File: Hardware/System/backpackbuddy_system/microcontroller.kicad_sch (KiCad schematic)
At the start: 10 parts

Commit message: more changes
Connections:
- net PD2 renamed PD2/RX
- net PD3 renamed PD3/TX
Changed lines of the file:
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@@
     (effects (font (size 1.27 1.27)) (justify left))
   )
-  (hierarchical_label "PD2" (shape bidirectional) (at 177.8 88.9 0)
+  (hierarchical_label "PD2{slash}RX" (shape bidirectional) (at 177.8 88.9 0)
     (effects (font (size 1.27 1.27)) (justify left))
   )
@@
     (effects (font (size 1.27 1.27)) (justify right))
   )
-  (hierarchical_label "PD3" (shape bidirectional) (at 177.8 91.44 0)
+  (hierarchical_label "PD3{slash}TX" (shape bidirectional) (at 177.8 91.44 0)
     (effects (font (size 1.27 1.27)) (justify left))
   )

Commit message: labels and stuff almost done
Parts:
- C? (x2): value 100nF -> 0.1uF; footprint (none) -> Capacitor_SMD:C_0603_1608Metric_Pad1.08x0.95mm_HandSolder; MPN (none) -> CAP CER 0.1UF 50V X7R 0603; Stock (none) -> https://www.digikey.com/en/products/detail/kemet/C0603C104K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
- C?: footprint (none) -> Capacitor_SMD:C_0805_2012Metric_Pad1.18x1.45mm_HandSolder; MPN (none) -> CAP CER 0805 1UF 16V X7R 5%; Stock (none) -> https://www.digikey.com/en/products/detail/kemet/C0805C105J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
- C? (x2): footprint (none) -> Capacitor_SMD:C_0805_2012Metric_Pad1.18x1.45mm_HandSolder; MPN (none) -> CAP CER 10PF 100V X8R 0805; Stock (none) -> https://www.digikey.com/en/products/detail/kemet/C0805C100J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
- R?: footprint (none) -> Resistor_SMD:R_0603_1608Metric_Pad0.98x0.95mm_HandSolder; MPN (none) -> RES 10K OHM 1% 1/10W 0603; Stock (none) -> https://www.digikey.com/en/products/detail/vishay-dale/CRCW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
- SW?: footprint (none) -> BackpackBuddyFootprintLibrary:RST_SW; MPN (none) -> HP0315AFKP2-R; Stock (none) -> https://www.digikey.com/en/products/detail/nkk-switches/HP0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
- U?: Stock (none) -> Ordered!
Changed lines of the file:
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@@
     (in_bom yes) (on_board yes)
     (property "Reference" "C?" (id 0) (at 139.7 26.67 0))
-    (property "Value" "100nF" (id 1) (at 139.7 29.21 0))
-    (property "Footprint" "" (id 2) (at 135.5852 31.75 0)
+    (property "Value" "0.1uF" (id 1) (at 139.7 29.21 0))
+    (property "Footprint" "Capacitor_SMD:C_0603_1608Metric_Pad1.08x0.95mm_HandSolder" (id 2) (at 135.5852 31.75 0)
       (effects (font (size 1.27 1.27)) hide)
     )
     (property "Datasheet" "~" (id 3) (at 134.62 27.94 0)
+      (effects (font (size 1.27 1.27)) hide)
+    )
+    (property "MPN" "CAP CER 0.1UF 50V X7R 0603" (id 4) (at 134.62 27.94 0)
+      (effects (font (size 1.27 1.27)) hide)
+    )
+    (property "Stock" "https://www.digikey.com/en/products/detail/kemet/C0603C104K5RAC3190/12701955?utm_adgroup=Capacitors&utm_source=google&utm_medium=cpc&utm_campaign=Shopping_Supplier_KEMET&utm_term=&utm_content=Capacitors" (id 5) (at 134.62 27.94 0)
       (effects (font (size 1.27 1.27)) hide)
     )
@@
     (property "Reference" "C?" (id 0) (at 133.35 90.17 0))
     (property "Value" "1uF" (id 1) (at 133.35 92.71 0))
-    (property "Footprint" "" (id 2) (at 129.2352 95.25 0)
+    (property "Footprint" "Capacitor_SMD:C_0805_2012Metric_Pad1.18x1.45mm_HandSolder" (id 2) (at 129.2352 95.25 0)
       (effects (font (size 1.27 1.27)) hide)
     )
     (property "Datasheet" "~" (id 3) (at 128.27 91.44 0)
+      (effects (font (size 1.27 1.27)) hide)
+    )
+    (property "MPN" "CAP CER 0805 1UF 16V X7R 5%" (id 4) (at 128.27 91.44 0)
+      (effects (font (size 1.27 1.27)) hide)
+    )
+    (property "Stock" "https://www.digikey.com/en/products/detail/kemet/C0805C105J4RECAUTO/13228798?utm_adgroup=Capacitors&utm_source=google&utm_medium=cpc&utm_campaign=Shopping_Supplier_KEMET&utm_term=&utm_content=Capacitors" (id 5) (at 128.27 91.44 0)
       (effects (font (size 1.27 1.27)) hide)
     )
@@
     )
     (property "Datasheet" "http://ww1.microchip.com/downloads/en/DeviceDoc/Atmel-7766-8-bit-AVR-ATmega16U4-32U4_Datasheet.pdf" (id 3) (at 152.4 91.44 0)
+      (effects (font (size 1.27 1.27)) hide)
+    )
+    (property "Stock" "Ordered!" (id 4) (at 152.4 91.44 0)
       (effects (font (size 1.27 1.27)) hide)
     )
@@
       (effects (font (size 1.27 1.27)) (justify left))
     )
-    (property "Footprint" "" (id 2) (at 112.522 27.94 90)
+    (property "Footprint" "Resistor_SMD:R_0603_1608Metric_Pad0.98x0.95mm_HandSolder" (id 2) (at 112.522 27.94 90)
       (effects (font (size 1.27 1.27)) hide)
     )
     (property "Datasheet" "~" (id 3) (at 114.3 27.94 0)
+      (effects (font (size 1.27 1.27)) hide)
+    )
+    (property "MPN" "RES 10K OHM 1% 1/10W 0603" (id 4) (at 114.3 27.94 0)
+      (effects (font (size 1.27 1.27)) hide)
+    )
+    (property "Stock" "https://www.digikey.com/en/products/detail/vishay-dale/CRCW060310K0FKECC/12744930?utm_adgroup=Resistors&utm_source=google&utm_medium=cpc&utm_campaign=Shopping_Supplier_Vishay&utm_term=&utm_content=Resistors" (id 5) (at 114.3 27.94 0)
       (effects (font (size 1.27 1.27)) hide)
     )
@@
     (property "Reference" "C?" (id 0) (at 111.76 59.69 90))
     (property "Value" "10pF" (id 1) (at 111.76 62.23 90))
-    (property "Footprint" "" (id 2) (at 115.57 65.0748 0)
+    (property "Footprint" "Capacitor_SMD:C_0805_2012Metric_Pad1.18x1.45mm_HandSolder" (id 2) (at 115.57 65.0748 0)
       (effects (font (size 1.27 1.27)) hide)
     )
     (property "Datasheet" "~" (id 3) (at 111.76 66.04 0)
+      (effects (font (size 1.27 1.27)) hide)
+    )
+    (property "MPN" "CAP CER 10PF 100V X8R 0805" (id 4) (at 111.76 66.04 0)
+      (effects (font (size 1.27 1.27)) hide)
+    )
+    (property "Stock" "https://www.digikey.com/en/products/detail/kemet/C0805C100J1HAC7800/12723834?utm_adgroup=Capacitors&utm_source=google&utm_medium=cpc&utm_campaign=Shopping_Supplier_KEMET&utm_term=&utm_content=Capacitors" (id 5) (at 111.76 66.04 0)
       (effects (font (size 1.27 1.27)) hide)
     )
@@
     (property "Reference" "SW?" (id 0) (at 127 26.67 0))
     (property "Value" "SW_Push" (id 1) (at 127 29.21 0))
-    (property "Footprint" "" (id 2) (at 127 29.21 0)
-      (effects (font (size 1.27 1.27)) hide)
-    )
-    (property "Datasheet" "~" (id 3) (at 127 29.21 0)
+    (property "Footprint" "BackpackBuddyFootprintLibrary:RST_SW" (id 2) (at 127 29.21 0)
+      (effects (font (size 1.27 1.27)) hide)
+    )
+    (property "Datasheet" "https://www.nkkswitches.com/pdf/HP03-2.pdf" (id 3) (at 127 29.21 0)
+      (effects (font (size 1.27 1.27)) hide)
+    )
+    (property "MPN" "HP0315AFKP2-R" (id 4) (at 127 34.29 0)
+      (effects (font (size 1.27 1.27)) hide)
+    )
+    (property "Stock" "https://www.digikey.com/en/products/detail/nkk-switches/HP0315AFKP2-R/1242035" (id 5) (at 127 34.29 0)
       (effects (font (size 1.27 1.27)) hide)
     )
@@
     (property "Reference" "C?" (id 0) (at 111.76 49.53 90))
     (property "Value" "10pF" (id 1) (at 111.76 52.07 90))
-    (property "Footprint" "" (id 2) (at 115.57 54.9148 0)
+    (property "Footprint" "Capacitor_SMD:C_0805_2012Metric_Pad1.18x1.45mm_HandSolder" (id 2) (at 115.57 54.9148 0)
       (effects (font (size 1.27 1.27)) hide)
     )
@@
       (effects (font (size 1.27 1.27)) hide)
     )
+    (property "MPN" "CAP CER 10PF 100V X8R 0805" (id 4) (at 111.76 55.88 0)
+      (effects (font (size 1.27 1.27)) hide)
+    )
+    (property "Stock" "https://www.digikey.com/en/products/detail/kemet/C0805C100J1HAC7800/12723834?utm_adgroup=Capacitors&utm_source=google&utm_medium=cpc&utm_campaign=Shopping_Supplier_KEMET&utm_term=&utm_content=Capacitors" (id 5) (at 111.76 55.88 0)
+      (effects (font (size 1.27 1.27)) hide)
+    )
     (pin "1")
     (pin "2")
@@
     (in_bom yes) (on_board yes)
     (property "Reference" "C?" (id 0) (at 120.65 81.28 0))
-    (property "Value" "100nF" (id 1) (at 120.65 83.82 0))
-    (property "Footprint" "" (id 2) (at 116.5352 86.36 0)
+    (property "Value" "0.1uF" (id 1) (at 120.65 83.82 0))
+    (property "Footprint" "Capacitor_SMD:C_0603_1608Metric_Pad1.08x0.95mm_HandSolder" (id 2) (at 116.5352 86.36 0)
       (effects (font (size 1.27 1.27)) hide)
     )
@@
       (effects (font (size 1.27 1.27)) hide)
     )
+    (property "MPN" "CAP CER 0.1UF 50V X7R 0603" (id 4) (at 115.57 82.55 0)
+      (effects (font (size 1.27 1.27)) hide)
+    )
+    (property "Stock" "https://www.digikey.com/en/products/detail/kemet/C0603C104K5RAC3190/12701955?utm_adgroup=Capacitors&utm_source=google&utm_medium=cpc&utm_campaign=Shopping_Supplier_KEMET&utm_term=&utm_content=Capacitors" (id 5) (at 115.57 82.55 0)
+      (effects (font (size 1.27 1.27)) hide)
+    )

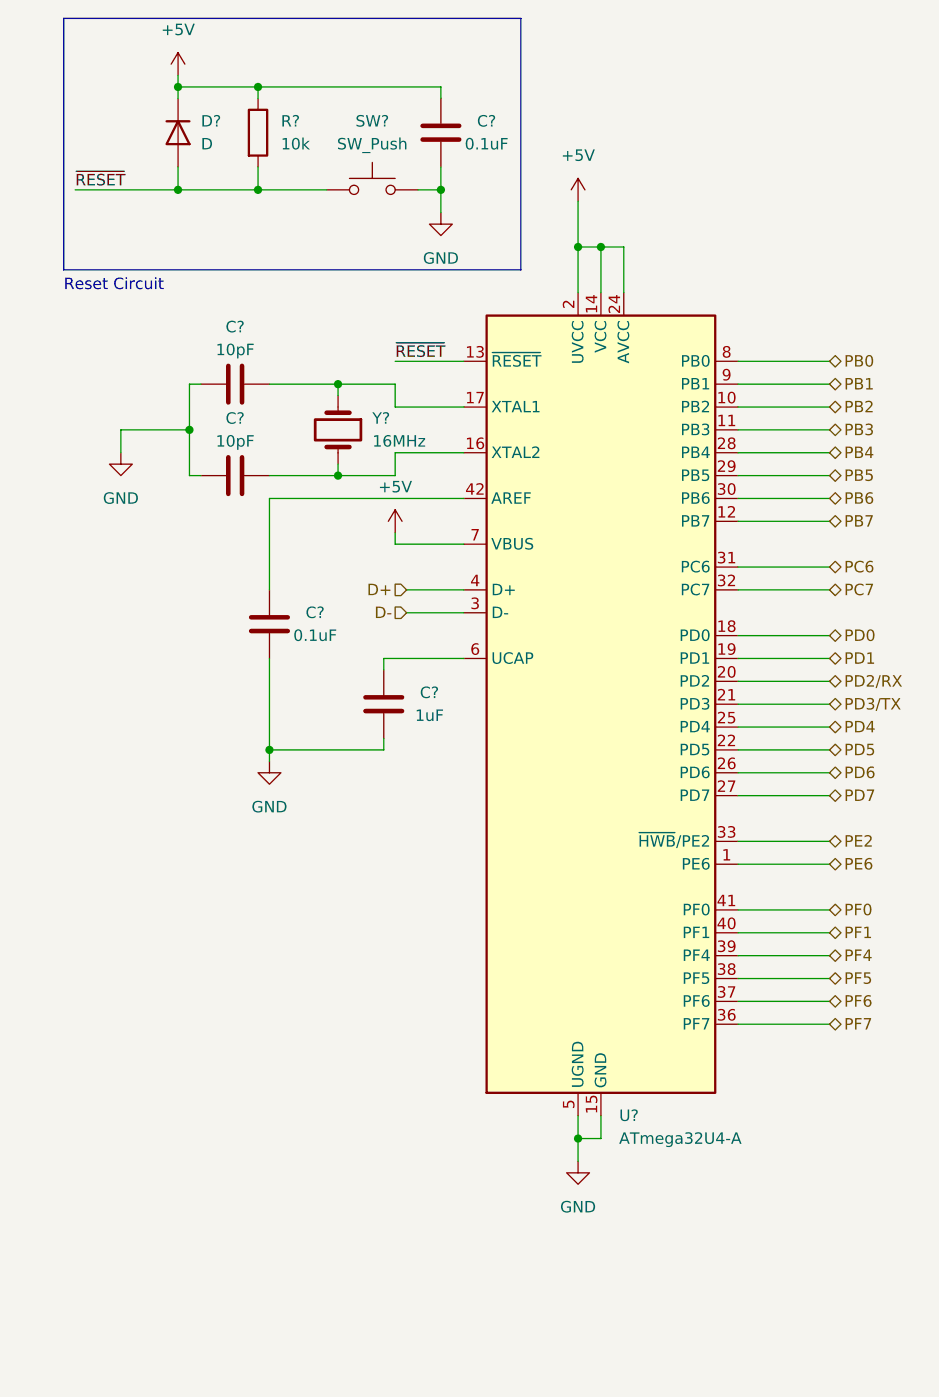
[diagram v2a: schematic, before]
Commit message: combining both sheets
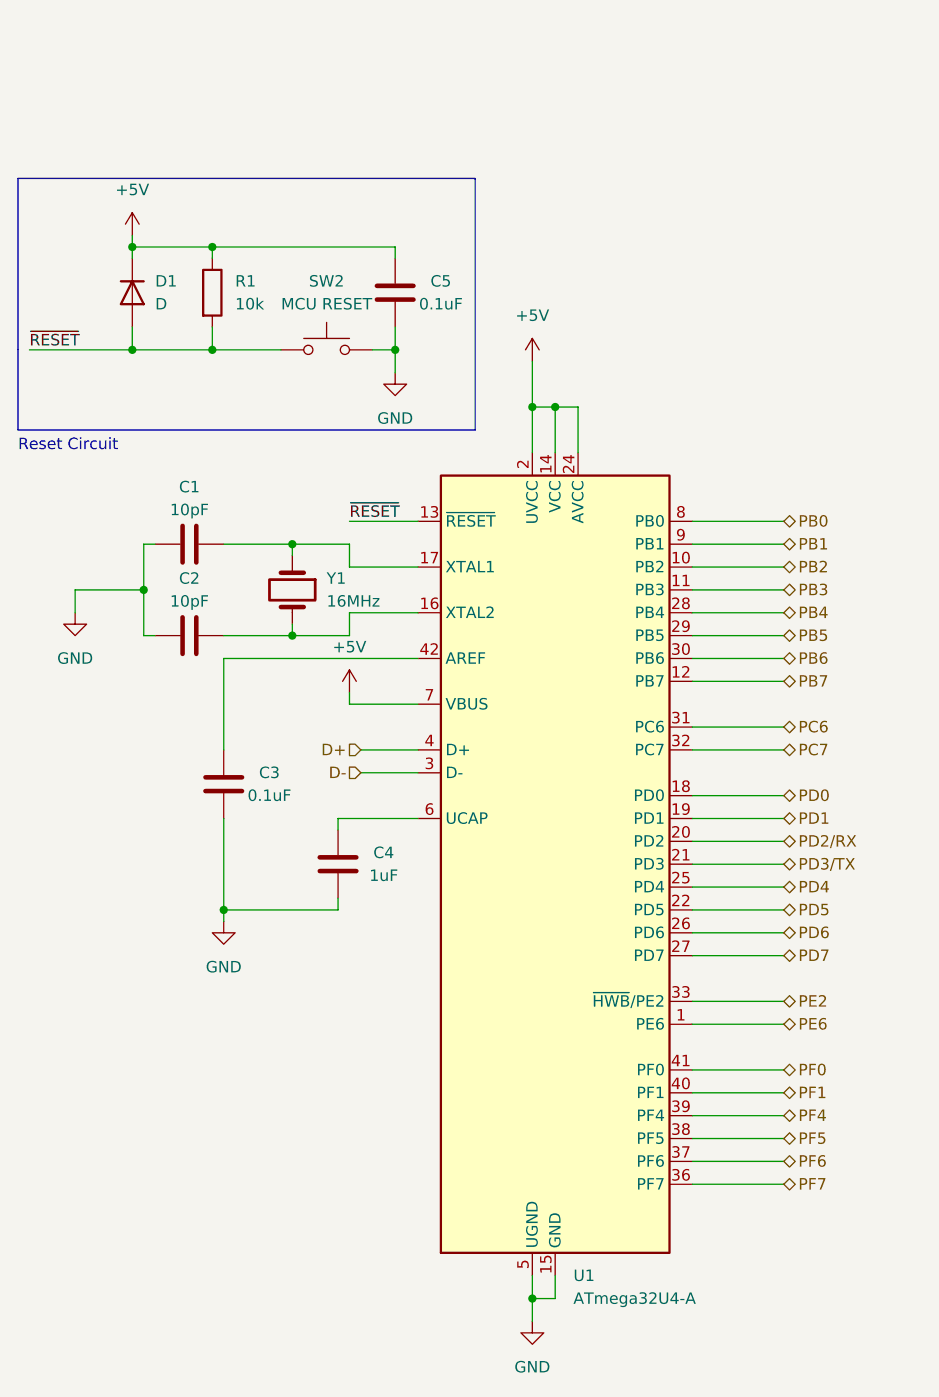
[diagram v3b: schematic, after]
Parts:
- SW2: renamed from SW?; value SW_Push -> MCU RESET
- gave numbers to parts that had none: 9
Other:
- moved on the sheet: C1, C2, C3, C4, C5, D1, R1, SW2, U1, Y1

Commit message: updated fields
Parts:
- Y1: footprint (none) -> Crystal:Crystal_SMD_3225-4Pin_3.2x2.5mm_HandSoldering; MPN (none) -> ABM8-16.000MHZ-7-1-U-T; Stock (none) -> https://www.digikey.com/en/products/detail/abracon-llc/ABM8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
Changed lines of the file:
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@@
       (effects (font (size 1.27 1.27)) (justify left))
     )
-    (property "Footprint" "" (id 2) (at 118.11 78.74 0)
+    (property "Footprint" "Crystal:Crystal_SMD_3225-4Pin_3.2x2.5mm_HandSoldering" (id 2) (at 118.11 78.74 0)
       (effects (font (size 1.27 1.27)) hide)
     )
-    (property "Datasheet" "~" (id 3) (at 118.11 78.74 0)
+    (property "Datasheet" "https://abracon.com/Resonators/abm8.pdf" (id 3) (at 118.11 78.74 0)
       (effects (font (size 1.27 1.27)) hide)
     )
+    (property "MPN" "ABM8-16.000MHZ-7-1-U-T" (id 4) (at 118.11 78.74 0)
+      (effects (font (size 1.27 1.27)) hide)
+    )
+    (property "Stock" "https://www.digikey.com/en/products/detail/abracon-llc/ABM8-16.000MHZ-7-1-U-T/5980142?utm_adgroup=Crystals&utm_source=google&utm_medium=cpc&utm_campaign=Shopping_Product_Crystals%2C%20Oscillators%2C%20Resonators_NEW&utm_term=&utm_content=Crystals" (id 5) (at 118.11 78.74 0)
+      (effects (font (size 1.27 1.27)) hide)
+    )
